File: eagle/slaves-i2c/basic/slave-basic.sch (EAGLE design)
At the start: 20 parts, among them CON3 SPI, IC3 MCP1703CB, J1 RJ12RIGHTANGLE-I2C, J2 RJ12RIGHTANGLE-I2C, U3 ATMEGA328

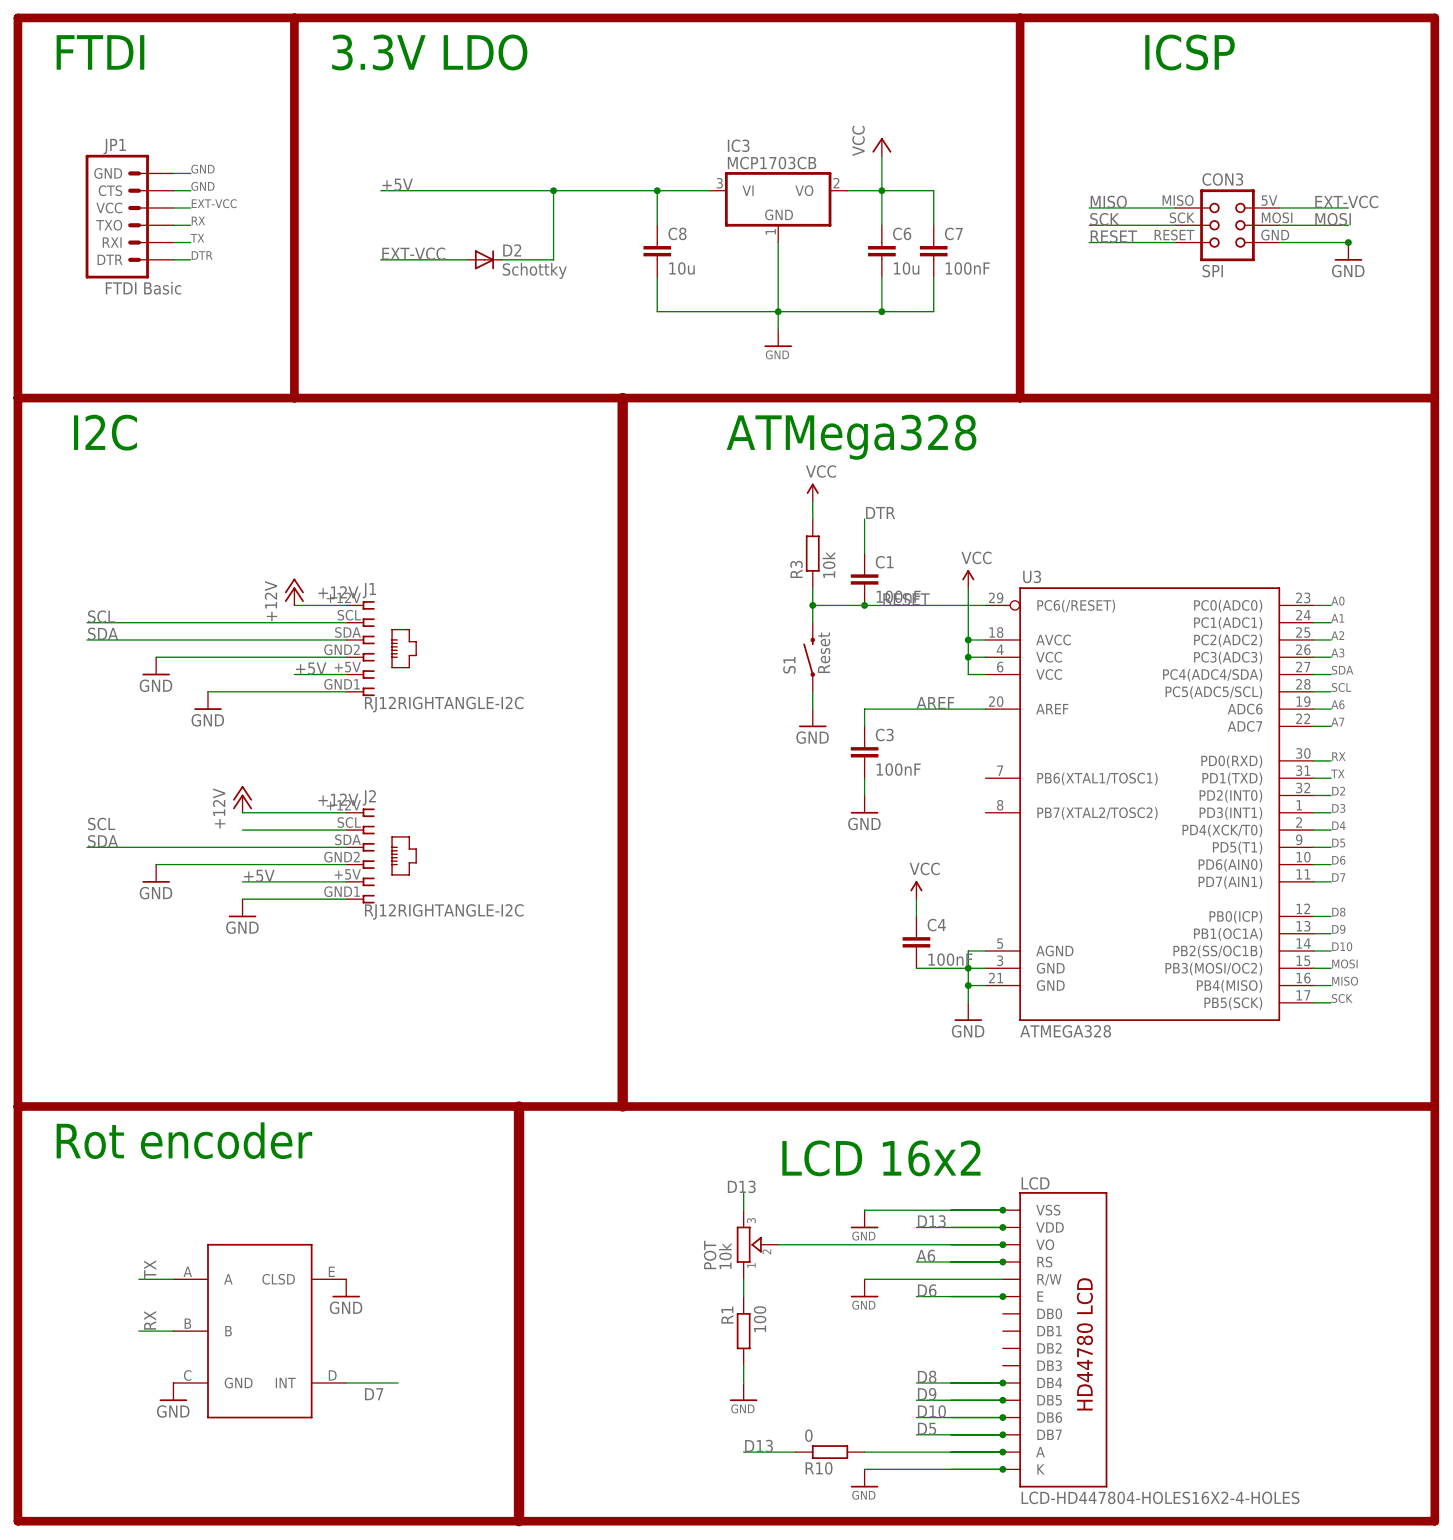
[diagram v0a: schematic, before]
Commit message: finish slave-basic
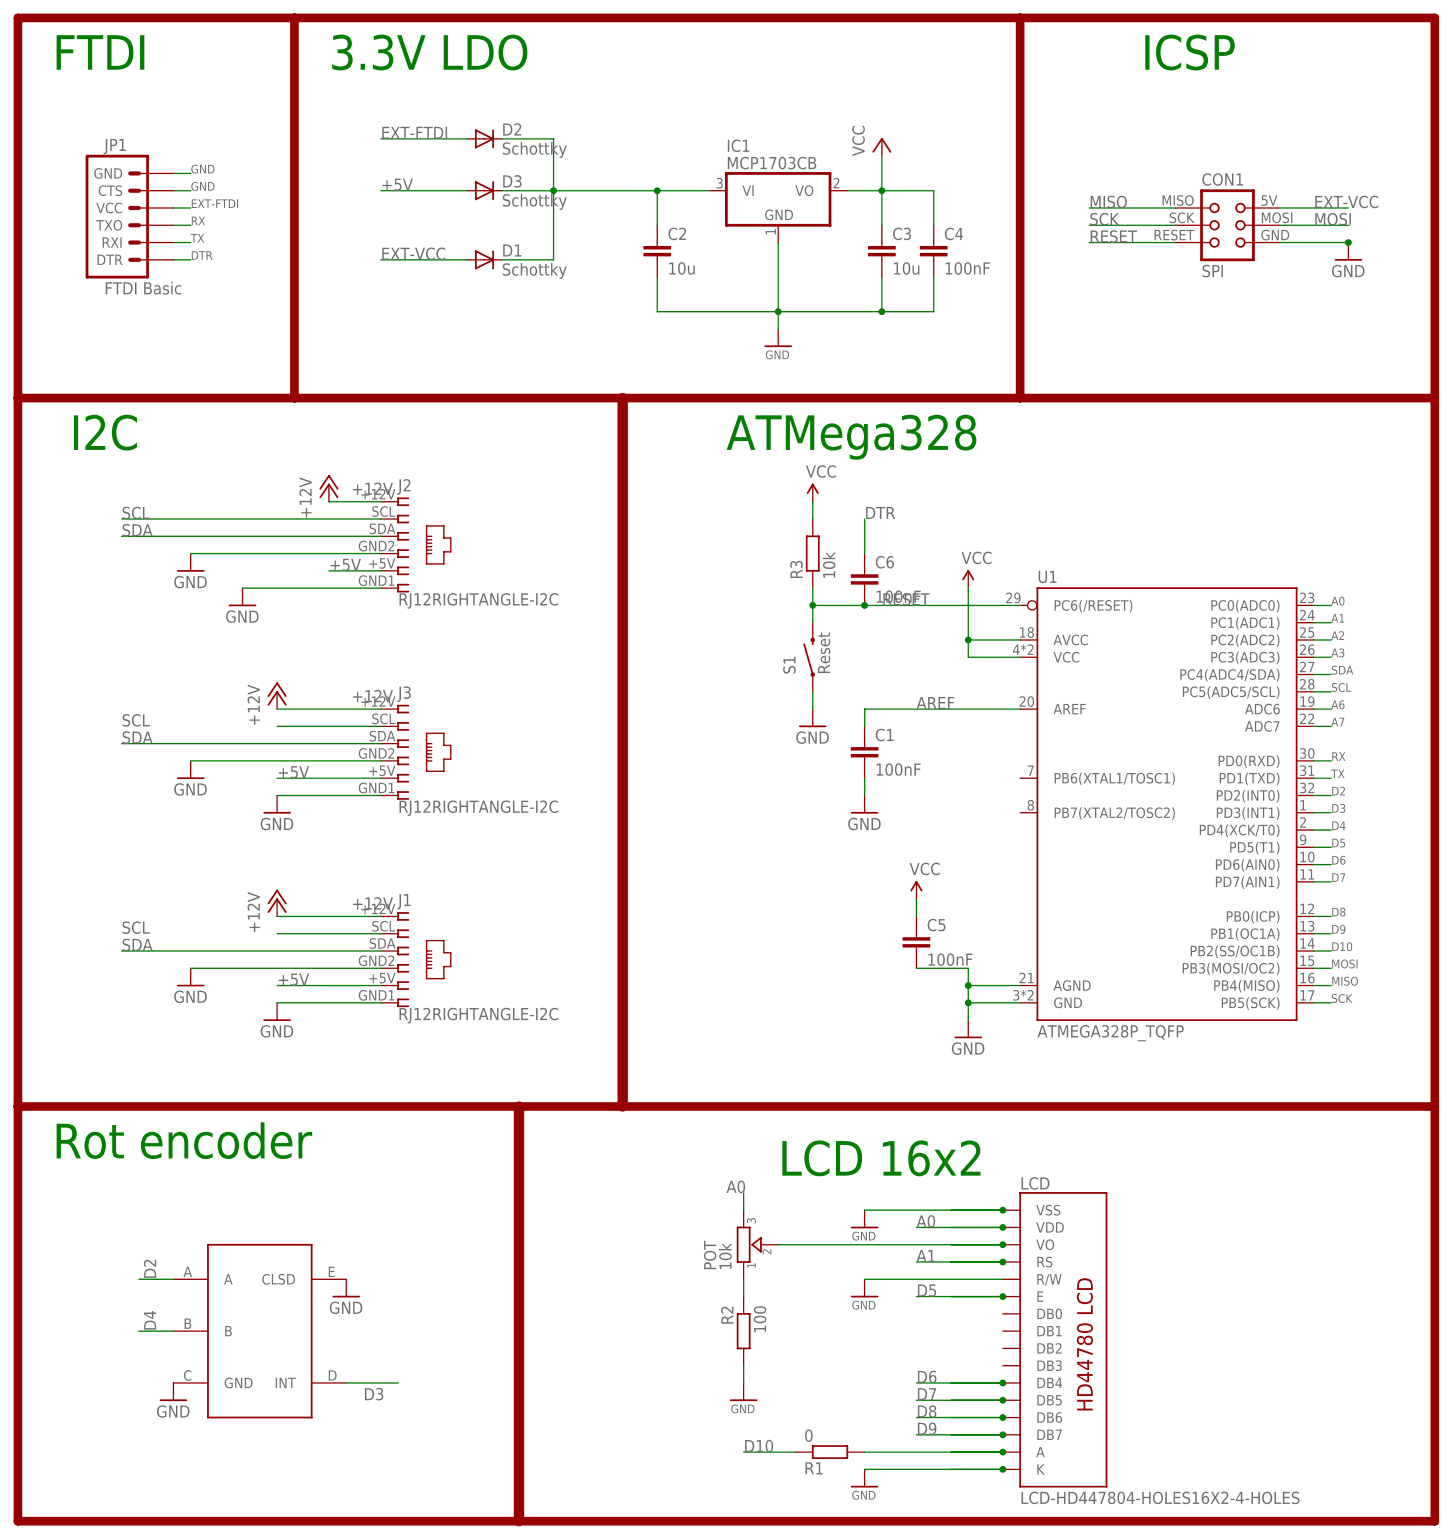
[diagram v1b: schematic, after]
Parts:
- removed C7: 100nF, rcl:C-EUC0805K
- removed R10: 0, rcl:R-EU_R0805
- removed U3: ATMEGA328, SparkFun:ATMEGA168
- added C5: 100nF, rcl:C-EUC0805K
- added D1, D3: Schottky, diode:MBR0520LT
- added J3: RJ12RIGHTANGLE-I2C, lpatiny:RJ12RIGHTANGLE-I2C
- added R2: 100, rcl:R-EU_R0805
- added U1: ATMEGA328P_TQFP, SparkFun-IC-Microcontroller:ATMEGA328P_TQFP
- C3: value 100nF -> 10u; ELECROW C49678 -> C15850; LCSC C49678 -> C15850; MPN 80-C1206C104K5R -> 77-VJ1206V106ZXQTBC
- C6: value 10u -> 100nF; ELECROW C15850 -> C49678; LCSC C15850 -> C49678; MPN 77-VJ1206V106ZXQTBC -> 80-C1206C104K5R
- R1: value 100 -> 0; ELECROW C17408 -> C17477; LCSC C17408 -> C17477
- renumbered C8 to C2, CON3 to CON1, IC3 to IC1
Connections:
- removed net D13: LCD.VDD, POT.3, R10.1
- new net +XV: C2.1, D1.C, D2.C, D3.C, IC1.VI
- new net EXT-FTDI: D2.A, JP1.VCC
- net +12V: now also J3.1
- net +5V: now also D3.A, J3.5; no longer C2.1, D2.C, IC1.VI
- net A0: now also LCD.VDD, POT.3, U1.PC0(ADC0); no longer U3.PC0(ADC0)
- net A1: now also LCD.RS, U1.PC1(ADC1); no longer U3.PC1(ADC1)
- net A2: now also U1.PC2(ADC2); no longer U3.PC2(ADC2)
- net A3: now also U1.PC3(ADC3); no longer U3.PC3(ADC3)
- net A6: now also U1.ADC6; no longer LCD.RS, U3.ADC6
- net A7: now also U1.ADC7; no longer U3.ADC7
- net AREF: now also C1.1, U1.AREF; no longer C3.1, U3.AREF
- net D10: now also R1.1, U1.PB2(SS/OC1B); no longer LCD.DB6, U3.PB2(SS/OC1B)
- net D2: now also U$1.A, U1.PD2(INT0); no longer U3.PD2(INT0)
- net D3: now also U$1.INT, U1.PD3(INT1); no longer U3.PD3(INT1)
- net D4: now also U$1.B, U1.PD4(XCK/T0); no longer U3.PD4(XCK/T0)
- net D5: now also LCD.E, U1.PD5(T1); no longer LCD.DB7, U3.PD5(T1)
- net D6: now also LCD.DB4, U1.PD6(AIN0); no longer LCD.E, U3.PD6(AIN0)
- net D7: now also LCD.DB5, U1.PD7(AIN1); no longer U$1.INT, U3.PD7(AIN1)
- net D8: now also LCD.DB6, U1.PB0(ICP); no longer LCD.DB4, U3.PB0(ICP)
- net D9: now also LCD.DB7, U1.PB1(OC1A); no longer LCD.DB5, U3.PB1(OC1A)
- net DTR: now also C6.1; no longer C1.1
- net EXT-VCC: now also D1.A; no longer D2.A, JP1.VCC
- net GND: now also C1.2, C5.2, J3.4, J3.6, R2.2, U1.AGND, U1.GND; no longer C6.2, C7.2, R1.2, U3.AGND, U3.GND@1, U3.GND@2
- net MISO: now also U1.PB4(MISO); no longer U3.PB4(MISO)
- net MOSI: now also U1.PB3(MOSI/OC2); no longer U3.PB3(MOSI/OC2)
- net N$11: now also R1.2; no longer R10.2
- net N$4: now also R2.1; no longer R1.1
- net RESET: now also C6.2, U1.PC6(/RESET); no longer C1.2, U3.PC6(/RESET)
- net RX: now also U1.PD0(RXD); no longer U$1.B, U3.PD0(RXD)
- net SCK: now also U1.PB5(SCK); no longer U3.PB5(SCK)
- net SCL: now also J3.2, U1.PC5(ADC5/SCL); no longer U3.PC5(ADC5/SCL)
- net SDA: now also J3.3, U1.PC4(ADC4/SDA); no longer U3.PC4(ADC4/SDA)
- net TX: now also U1.PD1(TXD); no longer U$1.A, U3.PD1(TXD)
- net VCC: now also C3.1, C5.1, U1.AVCC, U1.VCC; no longer C6.1, C7.1, U3.AVCC, U3.VCC@1, U3.VCC@2
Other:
- moved on the sheet: C1, C3, C4, C6, D2, J1, J2, R1
